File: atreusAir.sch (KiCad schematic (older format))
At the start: 90 parts, among them SW1 POWER, SW10 Push, SW11 Push, SW12 Push, SW13 Push, SW14 Push, SW15 Push, SW16 Push, SW17 Push, SW18 Push, SW19 Push, SW2 Push, SW20 Push, SW21 Push, SW22 Push, SW23 Push, SW24 Push, SW25 Push, SW26 Push, SW27 Push, SW28 Push, SW29 Push, SW3 Push, SW30 Push, SW31 Push, SW32 Push, SW33 Push, SW34 Push, SW35 Push, SW36 Push, SW37 Push, SW38 Push, SW39 Push, SW4 Push, SW40 Push, SW41 Push, SW42 Push, SW43 Push, SW5 Push, SW6 Push, SW7 Push, SW8 Push, SW9 Push, U1 Feather_Bluefruit_LE

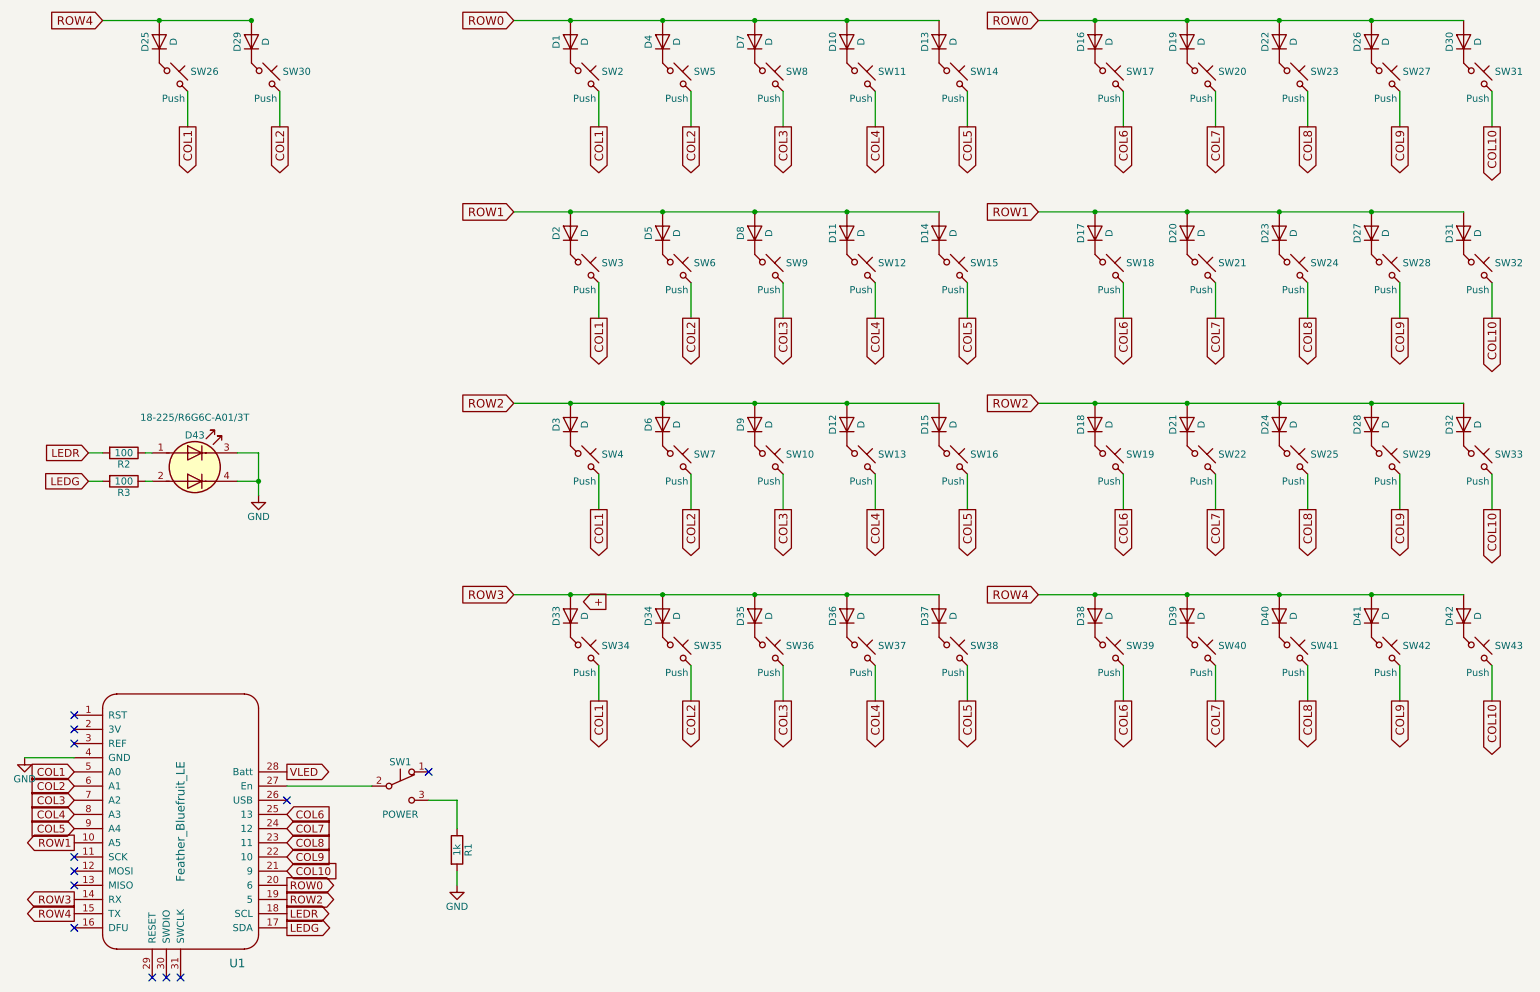
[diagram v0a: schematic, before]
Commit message: switches sorted but not yet connected
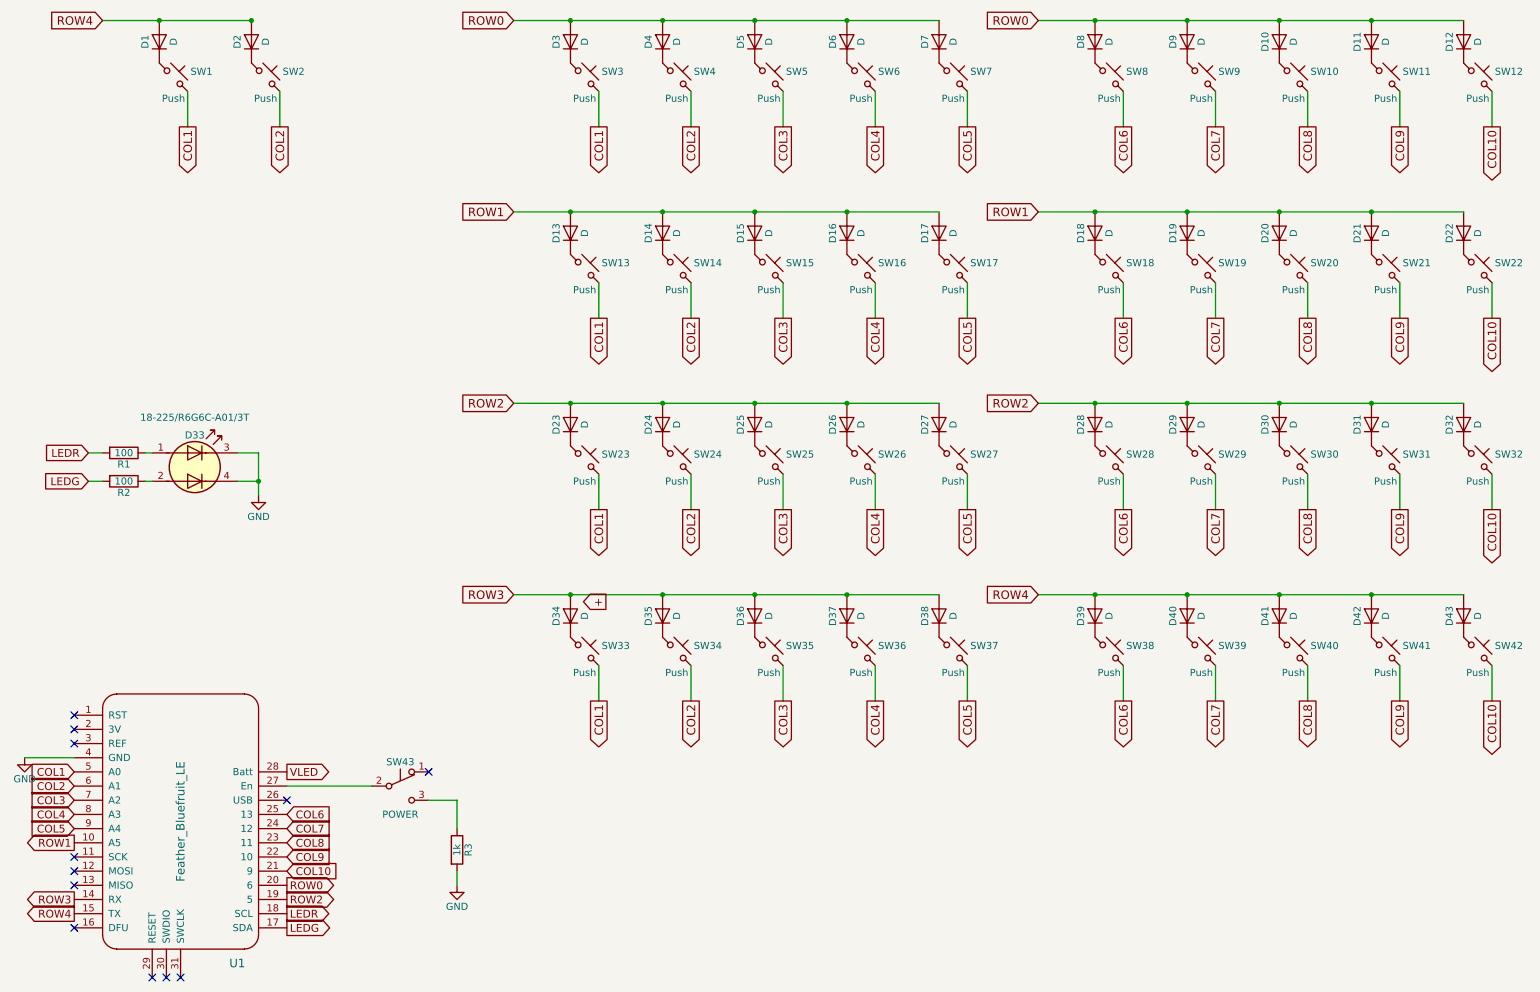
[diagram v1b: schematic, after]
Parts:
- renumbered D25 to D1, D22 to D10, D26 to D11, D30 to D12, D2 to D13, D5 to D14, D8 to D15, D11 to D16, D14 to D17, D17 to D18, D20 to D19, D29 to D2, D23 to D20, D27 to D21, D31 to D22, D3 to D23, D6 to D24, D9 to D25, D12 to D26, D15 to D27, D18 to D28, D21 to D29, D1 to D3, D24 to D30, D28 to D31, D43 to D33, D33 to D34, D34 to D35, D35 to D36, D36 to D37, D37 to D38, D38 to D39, D39 to D40, D40 to D41, D41 to D42, D42 to D43, D7 to D5, D10 to D6, D13 to D7, D16 to D8, D19 to D9, R2 to R1, R3 to R2, R1 to R3, SW26 to SW1, SW23 to SW10, SW27 to SW11, SW31 to SW12, SW3 to SW13, SW6 to SW14, SW9 to SW15, SW12 to SW16, SW15 to SW17, SW21 to SW19, SW30 to SW2, SW24 to SW20, SW28 to SW21, SW32 to SW22, SW4 to SW23, SW7 to SW24, SW10 to SW25, SW13 to SW26, SW16 to SW27, SW19 to SW28, SW22 to SW29, SW2 to SW3, SW25 to SW30, SW29 to SW31, SW33 to SW32, SW34 to SW33, SW35 to SW34, SW36 to SW35, SW37 to SW36, SW38 to SW37, SW39 to SW38, SW40 to SW39, SW5 to SW4, SW41 to SW40, SW42 to SW41, SW43 to SW42, SW1 to SW43, SW8 to SW5, SW11 to SW6, SW14 to SW7, SW17 to SW8, SW20 to SW9

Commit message: ausrichtung feather korrigiert ! !
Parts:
- renumbered D34 to D33, D35 to D34, D36 to D35, D37 to D36, D38 to D37, D39 to D38, D40 to D39, D41 to D40, D42 to D41, D43 to D42, D33 to D43, R3 to R1, R1 to R2, R2 to R3
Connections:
- net COL1: now also SW2.2; no longer SW1.2
- net COL2: no longer SW2.2
- net COL6: now also SW1.2
- net LEDG: now also R2.2; no longer R3.2
- net LEDR: now also R3.2; no longer R2.2
- net ROW0: now also D38.2 (A), D39.2 (A), D40.2 (A), D41.2 (A), D42.2 (A); no longer D10.2 (A), D11.2 (A), D12.2 (A), D8.2 (A), D9.2 (A)
- net ROW4: now also D10.2 (A), D11.2 (A), D12.2 (A), D8.2 (A), D9.2 (A); no longer D38.2 (A), D39.2 (A), D40.2 (A), D41.2 (A), D42.2 (A)
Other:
- moved on the sheet: D43, R2, R3
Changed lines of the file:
@@
 $EndDescr
 Text GLabel 7800 750  0    60   Input ~ 0
-ROW0
+ROW4
 $Comp
 L SW_Push_45deg SW8
@@
 Connection ~ 2250 750
 Text GLabel 1800 1500 3    60   Output ~ 0
+COL6
+Text GLabel 2450 1500 3    60   Output ~ 0
 COL1
-Text GLabel 2450 1500 3    60   Output ~ 0
-COL2
 Wire Wire Line
 	2450 1250 2450 1500
@@
 ROW2
 $Comp
-L GND #PWR3
+L GND #PWR01
 U 1 1 5B8A5396
 P 3700 6850
-F 0 "#PWR3" H 3700 6600 50  0001 C CNN
+F 0 "#PWR01" H 3700 6600 50  0001 C CNN
 F 1 "GND" H 3700 6700 50  0000 C CNN
 F 2 "" H 3700 6850 50  0000 C CNN
@@
 $EndComp
 $Comp
-L R R3
+L R R1
 U 1 1 5B8A5A88
 P 3700 6600
-F 0 "R3" V 3780 6600 50  0000 C CNN
+F 0 "R1" V 3780 6600 50  0000 C CNN
 F 1 "1k" V 3700 6600 50  0000 C CNN
 F 2 "Resistors_SMD:R_0603" V 3630 6600 50  0001 C CNN
@@
 COL10
 Text GLabel 7800 4800 0    60   Input ~ 0
-ROW4
+ROW0
 $Comp
 L SW_Push_45deg SW38
@@
 $EndComp
 $Comp
-L D D39
+L D D38
 U 1 1 5B8AFECD
 P 8200 4950
-F 0 "D39" H 8200 5050 50  0000 C CNN
+F 0 "D38" H 8200 5050 50  0000 C CNN
 F 1 "D" H 8200 4850 50  0000 C CNN
 F 2 "Diodes_SMD:D_0603" H 8200 4950 50  0001 C CNN
@@
 $EndComp
 $Comp
-L D D40
+L D D39
 U 1 1 5B8AFED3
 P 8850 4950
-F 0 "D40" H 8850 5050 50  0000 C CNN
+F 0 "D39" H 8850 5050 50  0000 C CNN
 F 1 "D" H 8850 4850 50  0000 C CNN
 F 2 "Diodes_SMD:D_0603" H 8850 4950 50  0001 C CNN
@@
 $EndComp
 $Comp
-L D D41
+L D D40
 U 1 1 5B8AFED9
 P 9500 4950
-F 0 "D41" H 9500 5050 50  0000 C CNN
+F 0 "D40" H 9500 5050 50  0000 C CNN
 F 1 "D" H 9500 4850 50  0000 C CNN
 F 2 "Diodes_SMD:D_0603" H 9500 4950 50  0001 C CNN
@@
 $EndComp
 $Comp
-L D D42
+L D D41
 U 1 1 5B8AFEDF
 P 10150 4950
-F 0 "D42" H 10150 5050 50  0000 C CNN
+F 0 "D41" H 10150 5050 50  0000 C CNN
 F 1 "D" H 10150 4850 50  0000 C CNN
 F 2 "Diodes_SMD:D_0603" H 10150 4950 50  0001 C CNN
@@
 $EndComp
 $Comp
-L D D43
+L D D42
 U 1 1 5B8AFEE5
 P 10800 4950
-F 0 "D43" H 10800 5050 50  0000 C CNN
+F 0 "D42" H 10800 5050 50  0000 C CNN
 F 1 "D" H 10800 4850 50  0000 C CNN
 F 2 "Diodes_SMD:D_0603" H 10800 4950 50  0001 C CNN
@@
 $EndComp
 $Comp
-L D D34
+L D D33
 U 1 1 5B8AFF18
 P 4500 4950
-F 0 "D34" H 4500 5050 50  0000 C CNN
+F 0 "D33" H 4500 5050 50  0000 C CNN
 F 1 "D" H 4500 4850 50  0000 C CNN
 F 2 "Diodes_SMD:D_0603" H 4500 4950 50  0001 C CNN
@@
 $EndComp
 $Comp
-L D D35
+L D D34
 U 1 1 5B8AFF1E
 P 5150 4950
-F 0 "D35" H 5150 5050 50  0000 C CNN
+F 0 "D34" H 5150 5050 50  0000 C CNN
 F 1 "D" H 5150 4850 50  0000 C CNN
 F 2 "Diodes_SMD:D_0603" H 5150 4950 50  0001 C CNN
@@
 $EndComp
 $Comp
-L D D36
+L D D35
 U 1 1 5B8AFF24
 P 5800 4950
-F 0 "D36" H 5800 5050 50  0000 C CNN
+F 0 "D35" H 5800 5050 50  0000 C CNN
 F 1 "D" H 5800 4850 50  0000 C CNN
 F 2 "Diodes_SMD:D_0603" H 5800 4950 50  0001 C CNN
@@
 $EndComp
 $Comp
-L D D37
+L D D36
 U 1 1 5B8AFF2A
 P 6450 4950
-F 0 "D37" H 6450 5050 50  0000 C CNN
+F 0 "D36" H 6450 5050 50  0000 C CNN
 F 1 "D" H 6450 4850 50  0000 C CNN
 F 2 "Diodes_SMD:D_0603" H 6450 4950 50  0001 C CNN
@@
 $EndComp
 $Comp
-L D D38
+L D D37
 U 1 1 5B8AFF30
 P 7100 4950
-F 0 "D38" H 7100 5050 50  0000 C CNN
+F 0 "D37" H 7100 5050 50  0000 C CNN
 F 1 "D" H 7100 4850 50  0000 C CNN
 F 2 "Diodes_SMD:D_0603" H 7100 4950 50  0001 C CNN
@@
 NoConn ~ 1000 5650
 $Comp
-L GND #PWR2
+L GND #PWR02
 U 1 1 5B9CD02C
 P 650 5950
-F 0 "#PWR2" H 650 5700 50  0001 C CNN
+F 0 "#PWR02" H 650 5700 50  0001 C CNN
 F 1 "GND" H 650 5800 50  0000 C CNN
 F 2 "" H 650 5950 50  0000 C CNN
@@
 Wire Wire Line
 	650  5950 1000 5950
-Text GLabel 1100 3800 0    55   Input ~ 0
+Text GLabel 4750 6850 0    55   Input ~ 0
 LEDR
-Text GLabel 1100 4000 0    55   Input ~ 0
+Text GLabel 4750 6650 0    55   Input ~ 0
 LEDG
 $Comp
-L GND #PWR1
+L GND #PWR03
 U 1 1 5BF50A4D
-P 2300 4100
-F 0 "#PWR1" H 2300 3850 50  0001 C CNN
-F 1 "GND" H 2300 3950 50  0000 C CNN
-F 2 "" H 2300 4100 50  0000 C CNN
-F 3 "" H 2300 4100 50  0000 C CNN
-	1    2300 4100
+P 5950 6950
+F 0 "#PWR03" H 5950 6700 50  0001 C CNN
+F 1 "GND" H 5950 6800 50  0000 C CNN
+F 2 "" H 5950 6950 50  0000 C CNN
+F 3 "" H 5950 6950 50  0000 C CNN
+	1    5950 6950
 	1    0    0    -1
 $EndComp
@@
 VLED
 $Comp
-L LED_Dual_AACC D33
+L LED_Dual_AACC D43
 U 1 1 5C14C150
-P 1850 3900
-F 0 "D33" H 1850 4125 50  0000 C CNN
-F 1 "18-225/R6G6C-A01/3T" H 1850 4250 50  0000 C CNN
-F 2 "atreusAir:R6G6C-A01" H 1880 3900 50  0001 C CNN
-F 3 "" H 1880 3900 50  0000 C CNN
-	1    1850 3900
-	1    0    0    -1
-$EndComp
-Wire Wire Line
-	2150 3800 2300 3800
-Wire Wire Line
-	2300 3800 2300 4100
-Wire Wire Line
-	2150 4000 2300 4000
-Connection ~ 2300 4000
-$Comp
-L R R1
+P 5500 6750
+F 0 "D43" H 5500 6975 50  0000 C CNN
+F 1 "18-225/R6G6C-A01/3T" H 5500 7100 50  0000 C CNN
+F 2 "atreusAir:R6G6C-A01" H 5530 6750 50  0001 C CNN
+F 3 "" H 5530 6750 50  0000 C CNN
+	1    5500 6750
+	1    0    0    -1
+$EndComp
+Wire Wire Line
+	5800 6650 5950 6650
+Wire Wire Line
+	5950 6650 5950 6950
+Wire Wire Line
+	5800 6850 5950 6850
+Connection ~ 5950 6850
+$Comp
+L R R2
 U 1 1 5C14C94E
-P 1350 3800
-F 0 "R1" V 1430 3800 50  0000 C CNN
-F 1 "100" V 1350 3800 50  0000 C CNN
-F 2 "Resistors_SMD:R_0603" V 1280 3800 50  0001 C CNN
-F 3 "" H 1350 3800 50  0000 C CNN
-	1    1350 3800
+P 5000 6650
+F 0 "R2" V 5080 6650 50  0000 C CNN
+F 1 "100" V 5000 6650 50  0000 C CNN
+F 2 "Resistors_SMD:R_0603" V 4930 6650 50  0001 C CNN
+F 3 "" H 5000 6650 50  0000 C CNN
+	1    5000 6650
 	0    1    1    0
 $EndComp
 $Comp
-L R R2
+L R R3
 U 1 1 5C14CA3D
-P 1350 4000
-F 0 "R2" V 1430 4000 50  0000 C CNN
-F 1 "100" V 1350 4000 50  0000 C CNN
-F 2 "Resistors_SMD:R_0603" V 1280 4000 50  0001 C CNN
-F 3 "" H 1350 4000 50  0000 C CNN
-	1    1350 4000
+P 5000 6850
+F 0 "R3" V 5080 6850 50  0000 C CNN
+F 1 "100" V 5000 6850 50  0000 C CNN
+F 2 "Resistors_SMD:R_0603" V 4930 6850 50  0001 C CNN
+F 3 "" H 5000 6850 50  0000 C CNN
+	1    5000 6850
 	0    1    1    0
 $EndComp
 Wire Wire Line
-	1500 4000 1550 4000
-Wire Wire Line
-	1500 3800 1550 3800
-Wire Wire Line
-	1100 3800 1200 3800
-Wire Wire Line
-	1100 4000 1200 4000
+	5150 6850 5200 6850
+Wire Wire Line
+	5150 6650 5200 6650
+Wire Wire Line
+	4750 6650 4850 6650
+Wire Wire Line
+	4750 6850 4850 6850
 $EndSCHEMATC

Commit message: feather jetzt auf unterseite, leiterbahnen verlegt.
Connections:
- net LEDG: now also R3.2; no longer R2.2
- net LEDR: now also R2.2; no longer R3.2
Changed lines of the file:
@@
 Wire Wire Line
 	650  5950 1000 5950
+Text GLabel 4750 6650 0    55   Input ~ 0
+LEDR
 Text GLabel 4750 6850 0    55   Input ~ 0
-LEDR
-Text GLabel 4750 6650 0    55   Input ~ 0
 LEDG
 $Comp
